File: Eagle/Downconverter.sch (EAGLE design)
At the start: 21 parts, among them J5 U.FL_CONN, J6 U.FL_CONN, U1 5V_REG, U2 MIXER, U3 DUAL_OP_AMP_LMV822, U4 DIGITAL_POTDIGITAL_POT

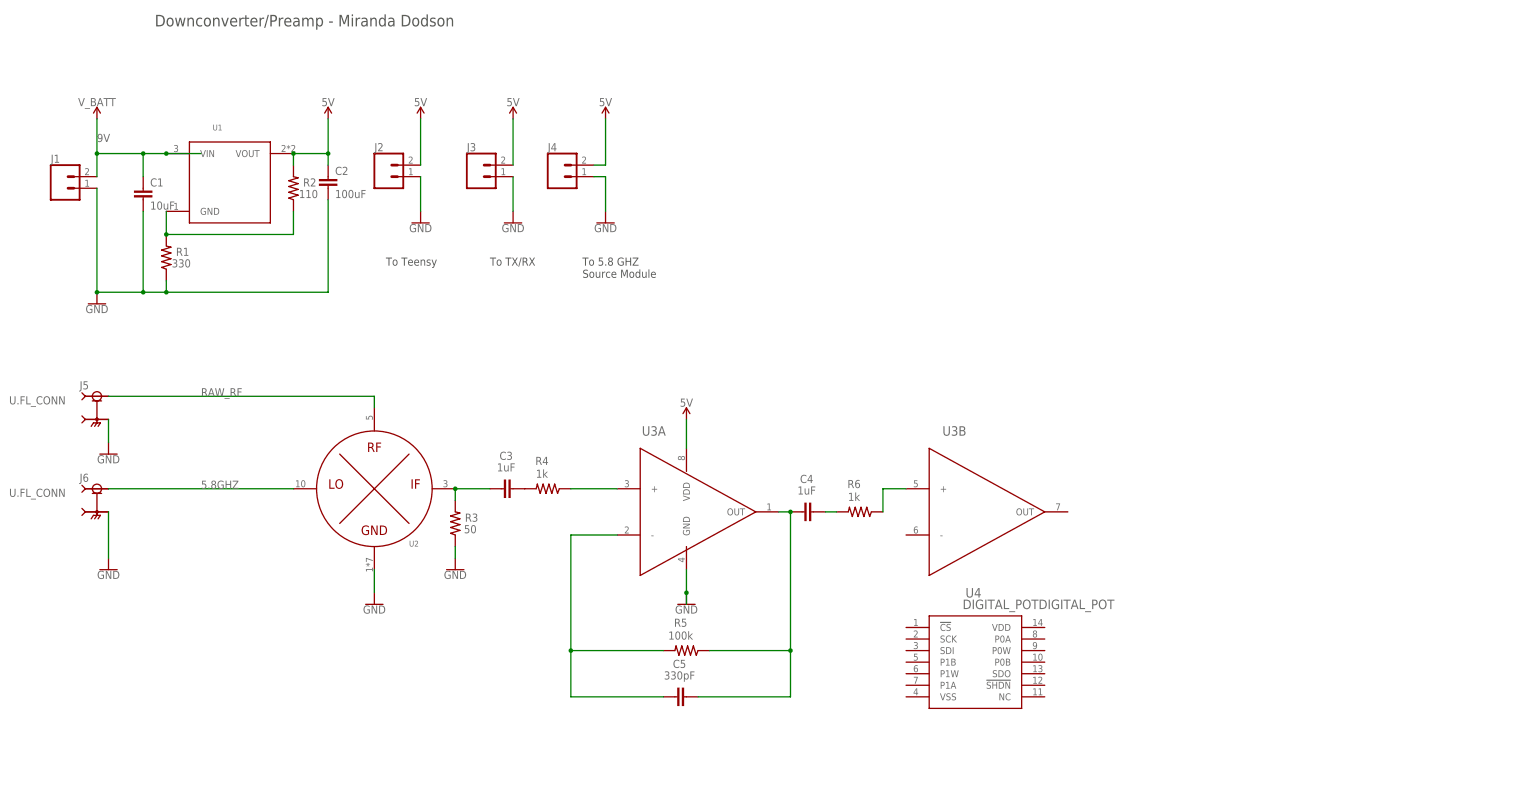
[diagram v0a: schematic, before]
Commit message: Progress
Just need to figure out how to do the audio jack, add some notes, and double check.
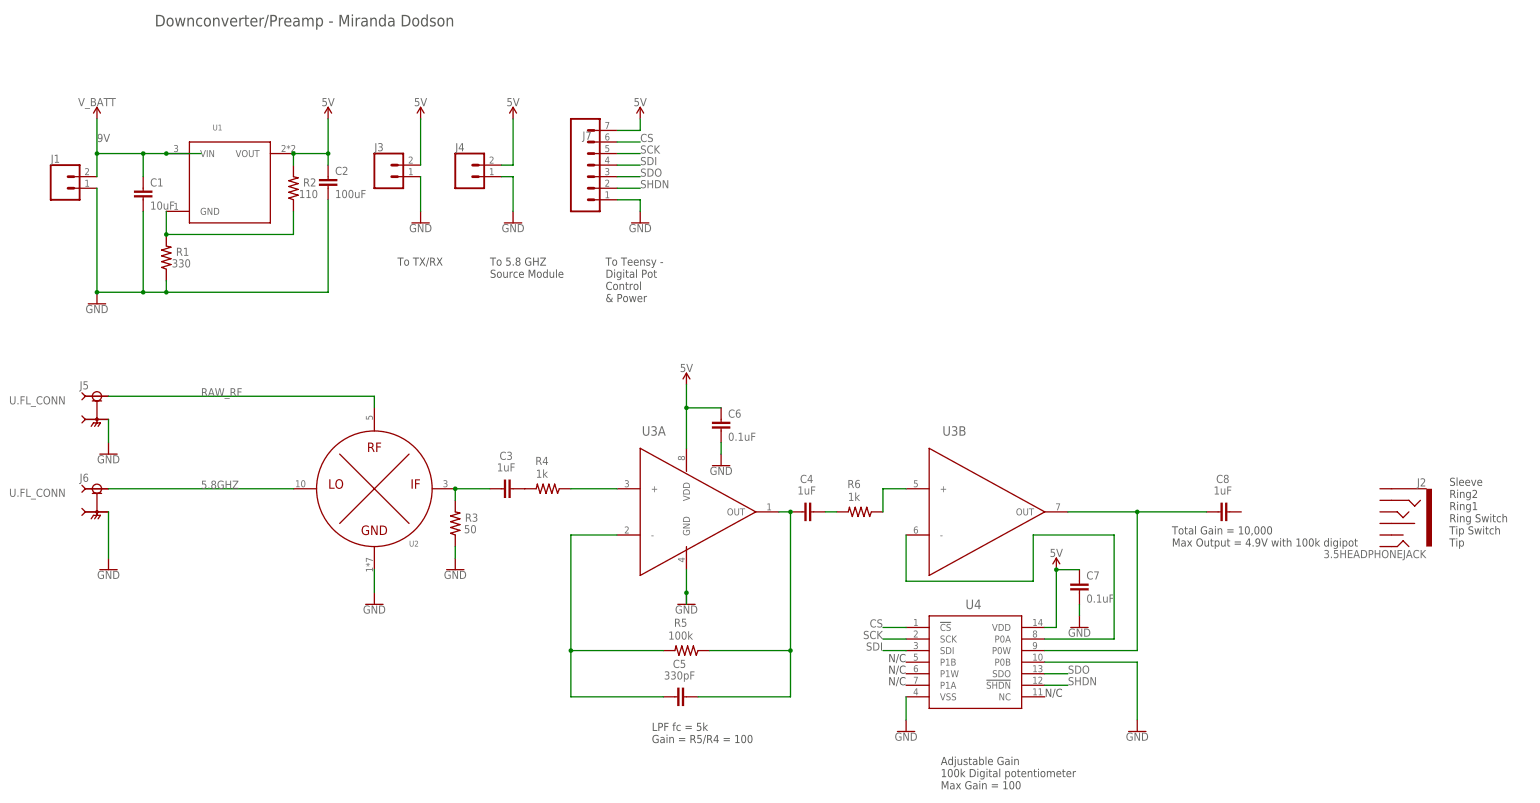
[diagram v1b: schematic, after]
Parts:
- added C6, C7: 0.1uF, 764Library:C0603
- added C8: 1uF, 764Library:C0603
- added J7: (no value), SparkFun-Connectors:CONN_07
- J2: value (none) -> 3.5HEADPHONEJACK; device SparkFun-Connectors:CONN_02 -> 764Library:3.5HEADPHONEJACK
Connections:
- new net CS: J7.6, U4.!CS
- new net N$12: C8.1, U3B.OUT, U4.P0W
- new net N$13: U3B.-, U4.P0A
- new net SCK: J7.5, U4.SCK
- new net SDI: J7.4, U4.SDI
- new net SDO: J7.3, U4.SDO
- new net SHDN: J7.2, U4.!SHDN
- net 5V: now also C6.1, C7.1, J7.7, U4.VDD; no longer J2.2
- net GND: now also C6.2, C7.2, J7.1, U4.P0B, U4.VSS; no longer J2.1
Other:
- note added: "Adjustable Gain 100k Digital potentiometer Max Gain = 100"
- note added: "LPF fc = 5k Gain = R5/R4 = 100"
- note added: "N/C"
- note added: "Sleeve Ring2 Ring1 Ring Switch Tip Switch Tip"
- note added: "To Teensy - Digital Pot Control & Power"
- note added: "Total Gain = 10,000 Max Output = 4.9V with 100k digipot"
- note removed: "To Teensy"
- moved on the sheet: J3, J4
